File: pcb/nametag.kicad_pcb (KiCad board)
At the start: 2 copper layers, 88 x 55 mm, 33 parts, among them J1 Conn_01x04, SW1 TS-1088-AR02016, U1 STC8H1K08-TSSOP20, U2 BL8536CB3TR36

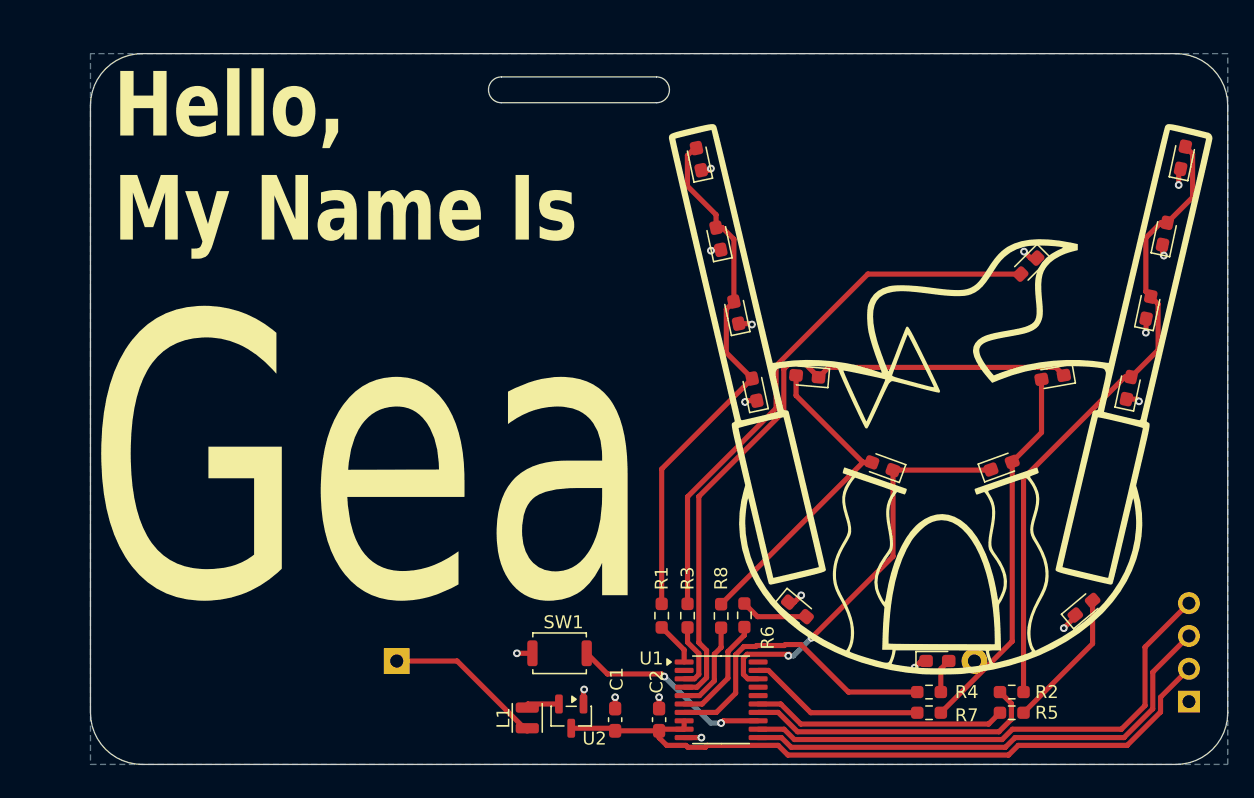
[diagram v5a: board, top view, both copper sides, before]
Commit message: Try swapping to a qfn part instead of tssop-20
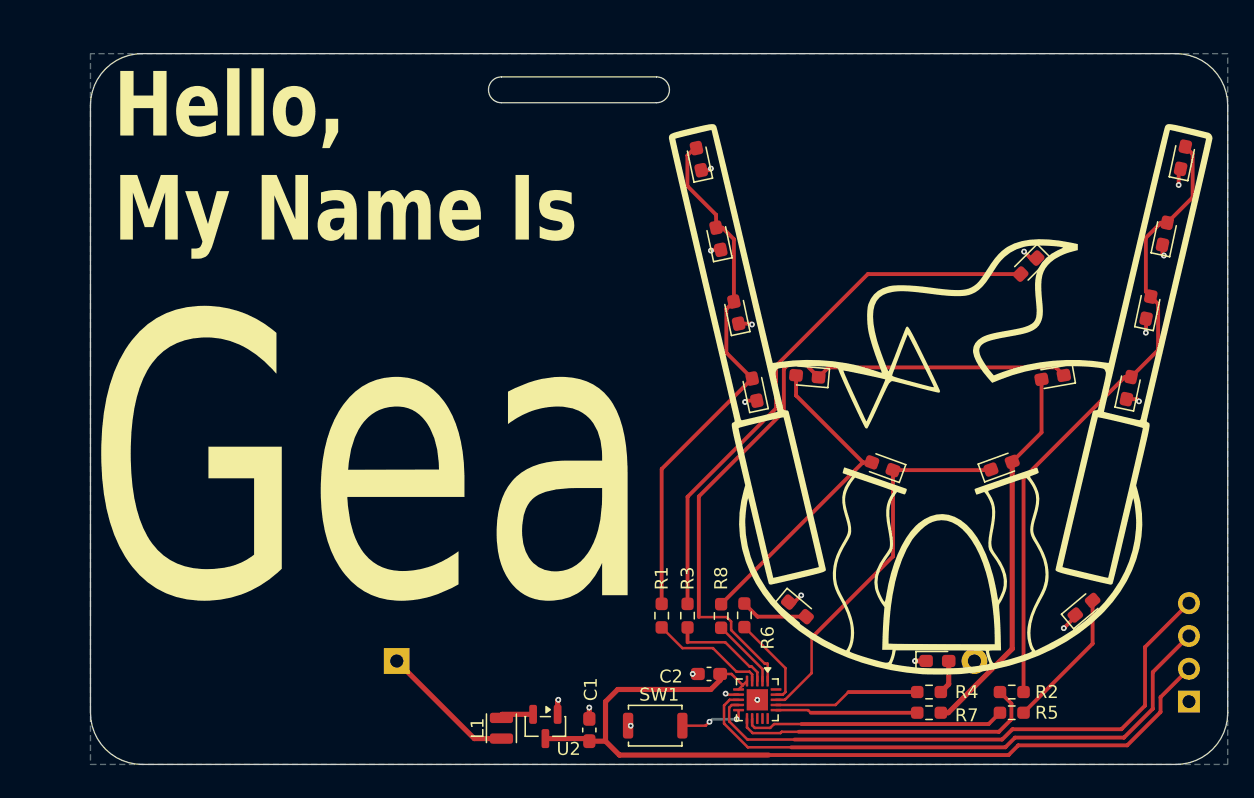
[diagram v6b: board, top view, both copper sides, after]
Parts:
- removed U1: STC8H1K08-TSSOP20, Package_SO:TSSOP-20_4.4x6.5mm_P0.65mm
- added U3: STC8H1K08-QFN20, Package_DFN_QFN:QFN-20-1EP_3x3mm_P0.4mm_EP1.65x1.65mm, F.Cu at (83.6, 90.0)
- moved SW1 9.28 mm to (75.7, 92.0)
- moved C2 5.24 mm to (79.9, 88.0), turned to 180 degrees
- moved C1 2.15 mm to (70.6, 92.3)
- moved L1 2.15 mm to (63.8, 92.2)
- moved U2 2.15 mm to (67.2, 92.1)
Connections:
- R1 pad 1: /Mcu/pwm2 -> /Mcu/pwm6
- R3 pad 1: /Mcu/pwm3 -> /Mcu/pwm5
- R4 pad 1: /Mcu/pwm6 -> /Mcu/pwm3
- R6 pad 1: /Mcu/pwm5 -> /Mcu/pwm2
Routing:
- net +3.3V: track 55.2 -> 69.9 mm
- net /Mcu/pwm6: track 23.5 -> 9.02 mm
- net /Mcu/switch: track 15.6 -> 5.17 mm
- net /Mcu/pwm3: track 5.28 -> 11.3 mm
- net /Mcu/UART_RX: track 38.9 -> 44.7 mm
- net /Mcu/UART_TX: track 40.7 -> 45.1 mm
- net /Mcu/pwm2: track 3.39 -> 7.15 mm
- net /Mcu/pwm1: track 13.7 -> 11.0 mm
- net /Mcu/cathode0: track 31.9 -> 29.5 mm, vias 2 -> 0
- net Net-(BT1-+): track 12.3 -> 10.6 mm
- net /Mcu/pwm4: track 7.19 -> 5.45 mm
- net /Mcu/cathode1: track 51.7 -> 53.3 mm
- net GND: track 18.3 -> 16.8 mm, vias 17 -> 18
- net /Mcu/pwm7: track 23.1 -> 24.2 mm
- net /Mcu/pwm8: track 19.7 -> 20.3 mm
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
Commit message: Add JLC PCBA Mounting holes
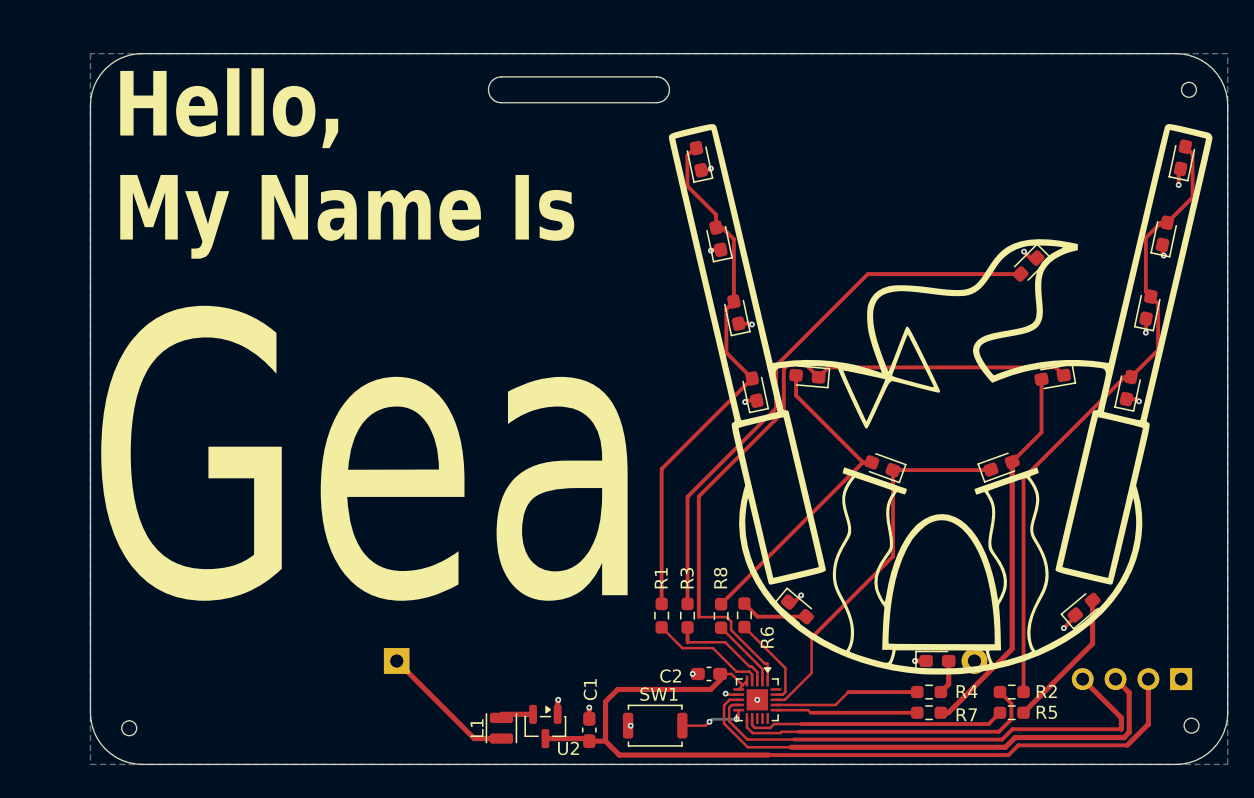
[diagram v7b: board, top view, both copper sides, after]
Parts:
- added REF**: JLC PCBA Mounting Hole, jlcpcb:JLC PCBA Mounting Hole, F.Cu at (117.2, 92.0)
- added REF**: JLC PCBA Mounting Hole, jlcpcb:JLC PCBA Mounting Hole, F.Cu at (35.0, 92.2)
- added REF**: JLC PCBA Mounting Hole, jlcpcb:JLC PCBA Mounting Hole, F.Cu at (117.0, 42.8)
- moved J1 1.84 mm to (116.4, 88.4), turned to 90 degrees
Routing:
- net /Mcu/UART_TX: track 45.1 -> 38.3 mm
- net /Mcu/UART_RX: track 44.7 -> 39.8 mm
- net +3.3V: track 69.9 -> 67.8 mm

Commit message: Enlarge the PCB a bit
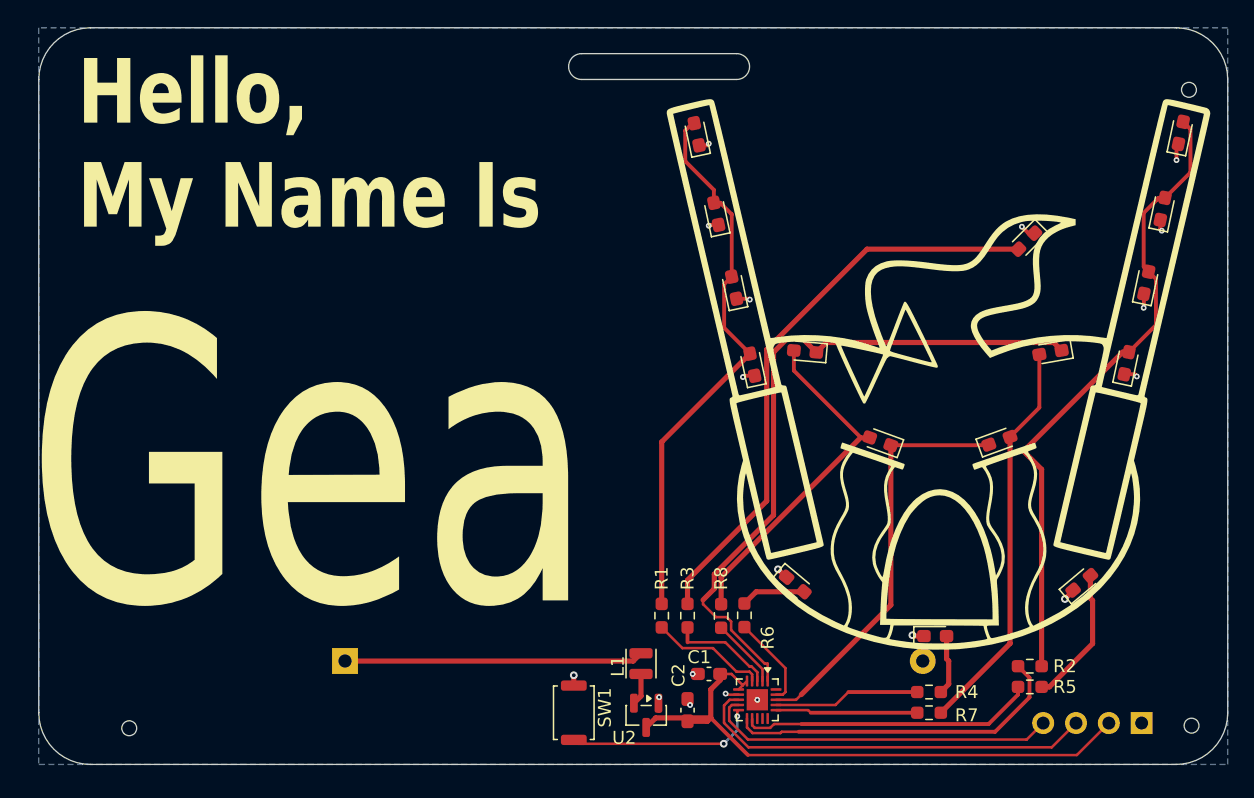
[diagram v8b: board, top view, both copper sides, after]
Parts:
- moved L1 11.9 mm to (74.6, 87.2), turned to -90 degrees
- moved U2 7.85 mm to (75.0, 91.2)
- moved C1 7.75 mm to (78.2, 90.8)
- moved SW1 6.38 mm to (69.4, 91.0), turned to 90 degrees
- moved J1 4.57 mm to (113.3, 91.8)
- moved BT1 4.00 mm to (51.7, 87.0)
- moved R2 2.44 mm to (104.7, 87.4)
- moved R5 2.44 mm to (104.7, 89.0)
- moved D5 1.93 mm to (116.4, 46.1)
- moved D7 1.93 mm to (113.7, 57.7)
- moved D8 1.93 mm to (112.2, 64.0)
- moved D1 1.93 mm to (78.9, 46.2)
- moved D12 1.93 mm to (87.3, 63.0)
- moved D16 1.93 mm to (93.1, 70.0)
- moved D4 1.93 mm to (83.2, 64.1)
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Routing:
- net +3.3V: track 67.8 -> 47.0 mm
- net Net-(BT1-+): track 10.6 -> 23.1 mm
- net /Mcu/UART_TX: track 38.3 -> 27.3 mm
- net /Mcu/switch: track 5.17 -> 14.8 mm
- net /Mcu/UART_RX: track 39.8 -> 31.5 mm
- net /Mcu/pwm8: track 20.3 -> 22.8 mm
- net /Mcu/pwm7: track 24.2 -> 26.7 mm
- net /Mcu/cathode0: track 29.5 -> 31.9 mm
- net Net-(D10-A): track 2.66 -> 4.65 mm
- net Net-(D1-A): track 41.2 -> 43.1 mm
- net Net-(D12-A): track 25.1 -> 26.9 mm
- net Net-(D9-A): track 43.1 -> 44.9 mm
- net Net-(D11-A): track 29.4 -> 30.9 mm
- net GND: track 16.8 -> 15.5 mm
- net /Mcu/cathode1: track 53.3 -> 54.1 mm
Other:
- board size 88 x 55 mm -> 92 x 57 mm
- board text added: "- + R T"
- board text added: "© xchgeaxeax 2026"
